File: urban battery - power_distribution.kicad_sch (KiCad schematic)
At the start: 18 parts, among them J1 FRONT_ACC_OUT, J2 12V_IN, J3 12VHC_OUT_EXTRA, J4 TEL_OUT, J5 REAR_ACC_OUT, J6 MTR_CTRL_OUT, J7 12VLC_OUT_EXTRA, J8 12VLC_OUT_EXTRA, J9 12VLC_OUT_EXTRA

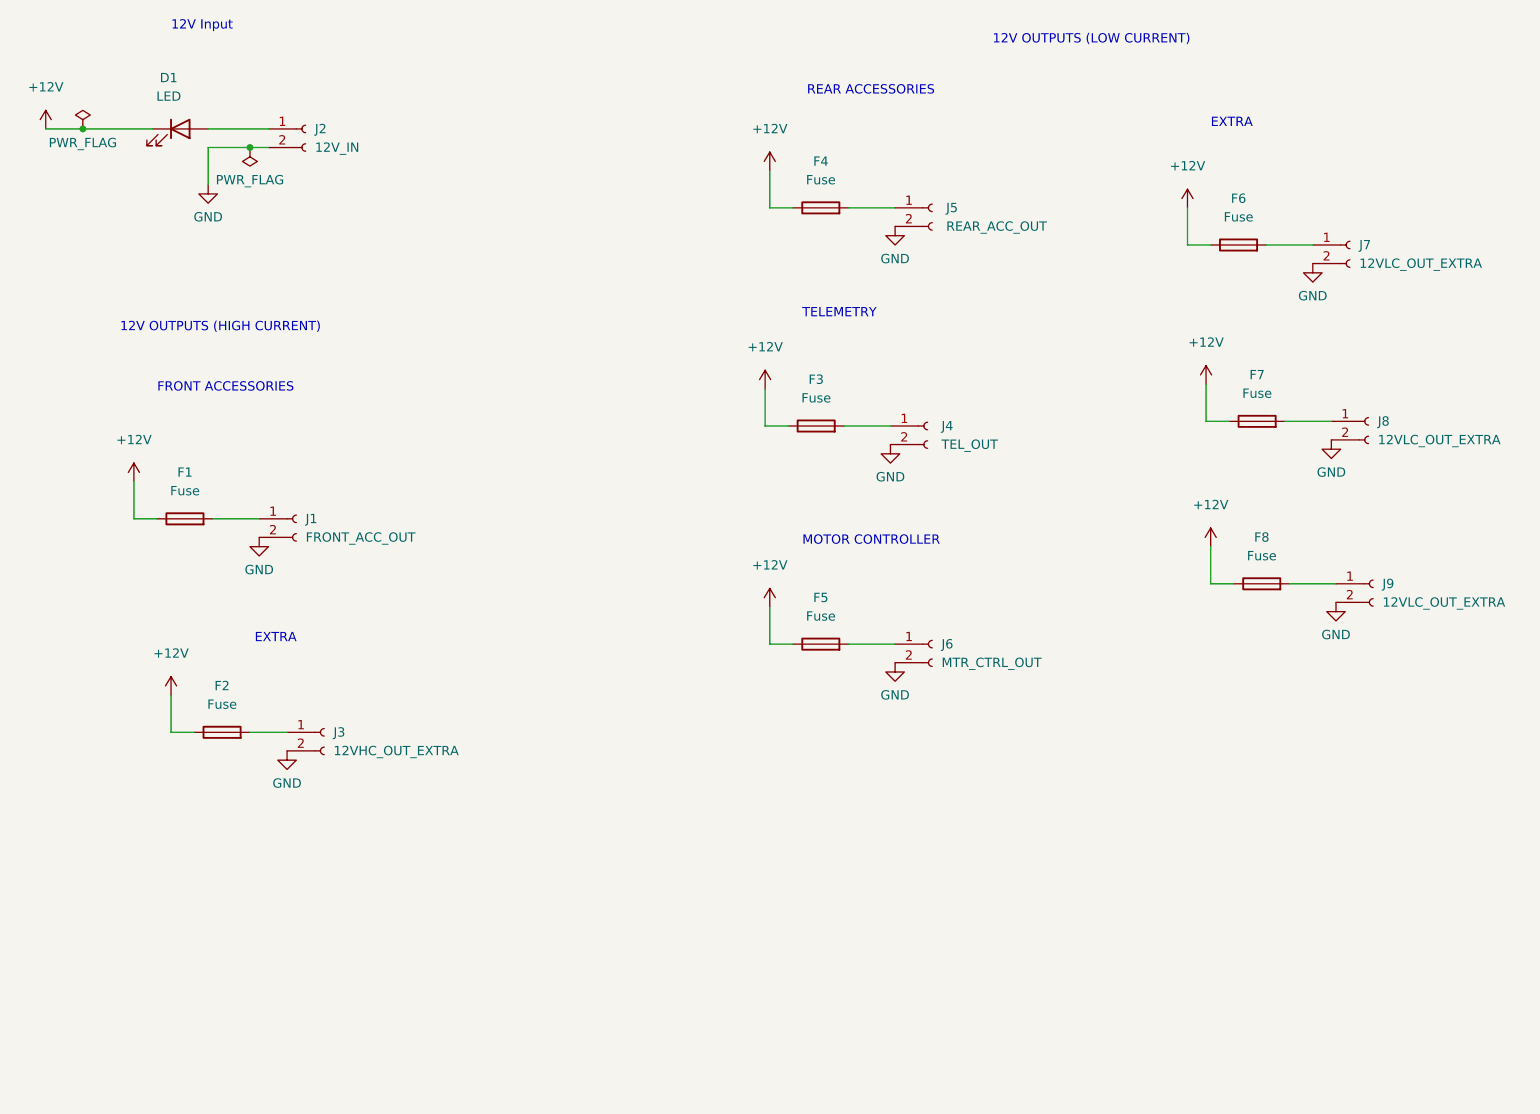
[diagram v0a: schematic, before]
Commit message: Assigned footprints and datasheets to every component
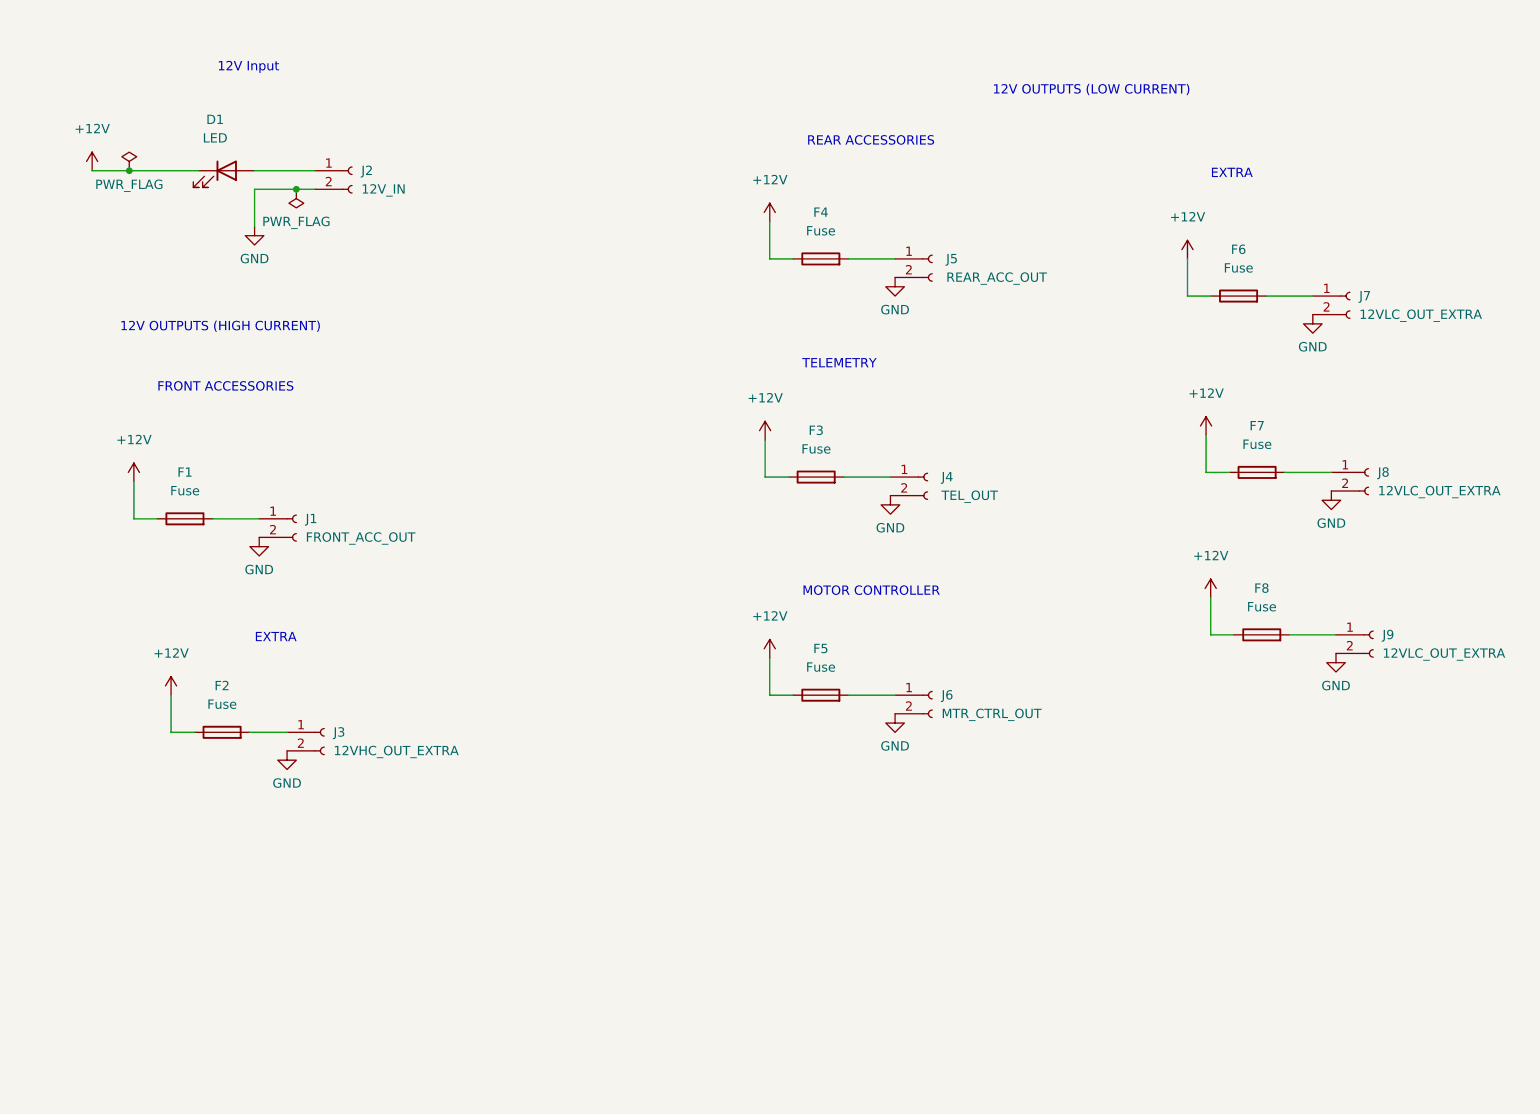
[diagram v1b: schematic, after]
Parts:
- F1, F2, F3, F4, F5, F6, F7, F8: footprint (none) -> Fuse:Fuseholder_Blade_Mini_Keystone_3568
- J1, J2, J3: footprint (none) -> urban-power-dist-pcb-custom-footprints:MOLEX_2002411222
- J4, J5, J6, J7, J8, J9: footprint (none) -> Connector_Molex:Molex_Micro-Fit_3.0_43650-0200_1x02_P3.00mm_Horizontal
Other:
- moved on the sheet: D1, F3, F4, F5, F6, F7, F8, J2, J4, J5, J6, J7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

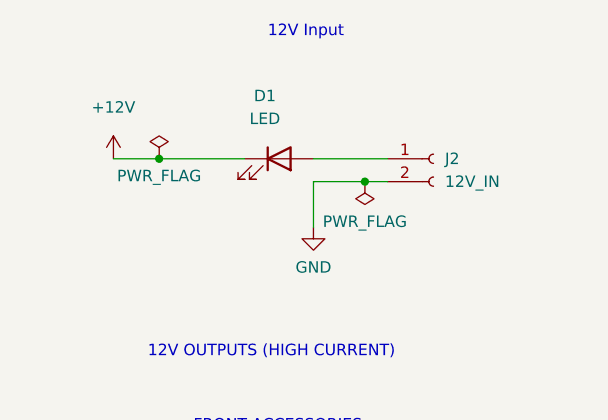
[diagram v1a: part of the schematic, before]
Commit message: added shunt resistor in front of LED and did most of layout
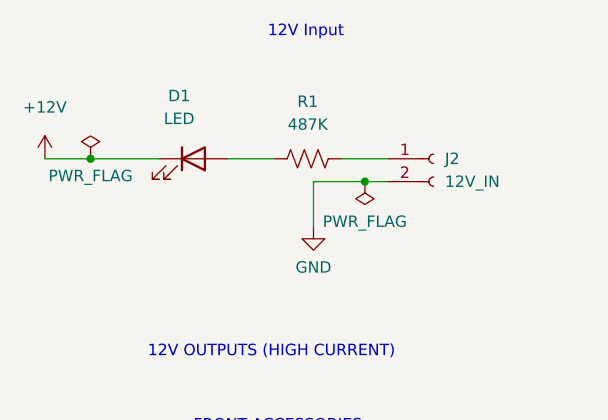
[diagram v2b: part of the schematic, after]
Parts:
- added R1: 487K, Resistor_SMD:R_0805_2012Metric, symbol Device:R_US
- D1: footprint (none) -> LED_SMD:LED_1206_3216Metric
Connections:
- net at D1.2 (A): now also R1.1; no longer J2.1 (Pin_1)
- new net: J2.1 (Pin_1), R1.2
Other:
- moved on the sheet: D1
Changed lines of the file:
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@@
   (junction (at 76.2 62.23) (diameter 0) (color 0 0 0 0)
   )
-  (junction (at 53.34 59.69) (diameter 0) (color 0 0 0 0)
+  (junction (at 45.72 59.69) (diameter 0) (color 0 0 0 0)
   )
   (wire (pts (xy 144.145 131.445) (xy 140.97 131.445))
@@
     (stroke (width 0) (type default) (color 0 0 0 0))
   )
-  (wire (pts (xy 70.485 59.69) (xy 78.74 59.69))
+  (wire (pts (xy 73.66 59.69) (xy 78.74 59.69))
     (stroke (width 0) (type default) (color 0 0 0 0))
   )
@@
     (stroke (width 0) (type default) (color 0 0 0 0))
   )
-  (wire (pts (xy 48.26 59.69) (xy 53.34 59.69))
+  (wire (pts (xy 40.64 59.69) (xy 45.72 59.69))
     (stroke (width 0) (type default) (color 0 0 0 0))
   )
@@
     (stroke (width 0) (type default) (color 0 0 0 0))
   )
-  (wire (pts (xy 53.34 59.69) (xy 62.865 59.69))
+  (wire (pts (xy 45.72 59.69) (xy 53.34 59.69))
     (stroke (width 0) (type default) (color 0 0 0 0))
   )
@@
   )
   (wire (pts (xy 203.835 100.965) (xy 200.66 100.965))
+    (stroke (width 0) (type default) (color 0 0 0 0))
+  )
+  (wire (pts (xy 60.96 59.69) (xy 66.04 59.69))
     (stroke (width 0) (type default) (color 0 0 0 0))
   )
@@
     (pin "2")
   )
-  (symbol (lib_id "Device:LED") (at 66.675 59.69 0) (unit 1)
-    (in_bom yes) (on_board yes) (fields_autoplaced)
-    (property "Reference" "D1" (id 0) (at 65.0875 52.705 0))
-    (property "Value" "LED" (id 1) (at 65.0875 55.245 0))
-    (property "Footprint" "" (id 2) (at 66.675 59.69 0)
-      (effects (font (size 1.27 1.27)) hide)
-    )
-    (property "Datasheet" "~" (id 3) (at 66.675 59.69 0)
+  (symbol (lib_id "Device:LED") (at 57.15 59.69 0) (unit 1)
+    (in_bom yes) (on_board yes)
+    (property "Reference" "D1" (id 0) (at 55.5625 52.705 0))
+    (property "Value" "LED" (id 1) (at 55.5625 55.245 0))
+    (property "Footprint" "LED_SMD:LED_1206_3216Metric" (id 2) (at 57.15 59.69 0)
+      (effects (font (size 1.27 1.27)) hide)
+    )
+    (property "Datasheet" "https://optoelectronics.liteon.com/upload/download/DS22-2000-026/LTST-C150TBKT(0630).pdf" (id 3) (at 57.15 59.69 0)
       (effects (font (size 1.27 1.27)) hide)
     )
@@
     (pin "1")
   )
-  (symbol (lib_id "power:PWR_FLAG") (at 53.34 59.69 0) (unit 1)
+  (symbol (lib_id "power:PWR_FLAG") (at 45.72 59.69 0) (unit 1)
     (in_bom yes) (on_board yes)
-    (property "Reference" "#FLG01" (id 0) (at 53.34 57.785 0)
-      (effects (font (size 1.27 1.27)) hide)
-    )
-    (property "Value" "PWR_FLAG" (id 1) (at 53.34 61.595 0))
-    (property "Footprint" "" (id 2) (at 53.34 59.69 0)
-      (effects (font (size 1.27 1.27)) hide)
-    )
-    (property "Datasheet" "~" (id 3) (at 53.34 59.69 0)
+    (property "Reference" "#FLG01" (id 0) (at 45.72 57.785 0)
+      (effects (font (size 1.27 1.27)) hide)
+    )
+    (property "Value" "PWR_FLAG" (id 1) (at 45.72 61.595 0))
+    (property "Footprint" "" (id 2) (at 45.72 59.69 0)
+      (effects (font (size 1.27 1.27)) hide)
+    )
+    (property "Datasheet" "~" (id 3) (at 45.72 59.69 0)
       (effects (font (size 1.27 1.27)) hide)
     )
@@
     (pin "1")
   )
-  (symbol (lib_id "power:+12V") (at 48.26 59.69 0) (unit 1)
-    (in_bom yes) (on_board yes) (fields_autoplaced)
-    (property "Reference" "#PWR01" (id 0) (at 48.26 63.5 0)
-      (effects (font (size 1.27 1.27)) hide)
-    )
-    (property "Value" "+12V" (id 1) (at 48.26 53.975 0))
-    (property "Footprint" "" (id 2) (at 48.26 59.69 0)
-      (effects (font (size 1.27 1.27)) hide)
-    )
-    (property "Datasheet" "" (id 3) (at 48.26 59.69 0)
+  (symbol (lib_id "Device:R_US") (at 69.85 59.69 90) (unit 1)
+    (in_bom yes) (on_board yes) (fields_autoplaced)
+    (property "Reference" "R1" (id 0) (at 69.85 53.34 90))
+    (property "Value" "487K" (id 1) (at 69.85 55.88 90))
+    (property "Footprint" "Resistor_SMD:R_0805_2012Metric" (id 2) (at 70.104 58.674 90)
+      (effects (font (size 1.27 1.27)) hide)
+    )
+    (property "Datasheet" "https://www.yageo.com/upload/media/product/productsearch/datasheet/rchip/PYu-RC_Group_51_RoHS_L_12.pdf" (id 3) (at 69.85 59.69 0)
+      (effects (font (size 1.27 1.27)) hide)
+    )
+    (pin "1")
+    (pin "2")
+  )
+  (symbol (lib_id "power:+12V") (at 40.64 59.69 0) (unit 1)
+    (in_bom yes) (on_board yes) (fields_autoplaced)
+    (property "Reference" "#PWR01" (id 0) (at 40.64 63.5 0)
+      (effects (font (size 1.27 1.27)) hide)
+    )
+    (property "Value" "+12V" (id 1) (at 40.64 53.975 0))
+    (property "Footprint" "" (id 2) (at 40.64 59.69 0)
+      (effects (font (size 1.27 1.27)) hide)
+    )
+    (property "Datasheet" "" (id 3) (at 40.64 59.69 0)
       (effects (font (size 1.27 1.27)) hide)
     )
@@
     )
     (path "/2d6e8602-341a-4e49-8f22-a4538a6c33d0"
-      (reference "D1") (unit 1) (value "LED") (footprint "")
+      (reference "D1") (unit 1) (value "LED") (footprint "LED_SMD:LED_1206_3216Metric")
     )
     (path "/b550b007-9a84-4bf0-930e-4eb2097f7f94"
@@
       (reference "J9") (unit 1) (value "12VLC_OUT_EXTRA") (footprint "Connector_Molex:Molex_Micro-Fit_3.0_43650-0200_1x02_P3.00mm_Horizontal")
     )
-  )
+    (path "/c61b44cb-28a5-4dfa-8f81-22358aec0d2e"
+      (reference "R1") (unit 1) (value "487K") (footprint "Resistor_SMD:R_0805_2012Metric")
+    )
+  )
